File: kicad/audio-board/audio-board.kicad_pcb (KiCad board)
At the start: 2 copper layers, 0 parts

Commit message: [LIMA] audio board: board setup — 4-layer, 70x50 outline, holes, netclasses
In1/In2 added (planes), Edge.Cuts 70x50 mm R1 at (100,80), 4x M3 at 3.5 mm
from corners. Rules for JLCPCB 4-layer: 0.127 track/clearance, 0.3/0.5 via.
Netclasses: Default 0.2/0.15, Power 0.5/0.2 (rails, switch nodes, A2B bias
path), Aircraft 0.3/0.5 clearance (panel, electret, PV secondary, speakers,
K1 contacts). No footprints yet: the schematic sync needs the PCB editor open.

Co-Authored-By: Claude Opus 5.5 <noreply@anthropic.com>
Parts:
- added H1: MountingHole, MountingHole:MountingHole_3.2mm, F.Cu at (103.5, 83.5)
- added H2: MountingHole, MountingHole:MountingHole_3.2mm, F.Cu at (166.5, 83.5)
- added H3: MountingHole, MountingHole:MountingHole_3.2mm, F.Cu at (103.5, 126.5)
- added H4: MountingHole, MountingHole:MountingHole_3.2mm, F.Cu at (166.5, 126.5)
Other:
- board outline added: 70 x 50 mm
- copper layers 2 -> 4
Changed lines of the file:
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@@
 		(48 "B.Fab" user)
 		(49 "F.Fab" user)
+		(1 "In1.Cu" power)
+		(2 "In2.Cu" power)
 	)
 	(setup
@@
 	)
 	(net 0 "")
-)
+  (gr_line
+    (start 100 80)
+    (end 170 80)
+    (stroke (width 0.05) (type solid))
+    (layer "Edge.Cuts")
+  )
+  (gr_line
+    (start 170 80)
+    (end 170 130)
+    (stroke (width 0.05) (type solid))
+    (layer "Edge.Cuts")
+  )
+  (gr_line
+    (start 170 130)
+    (end 100 130)
+    (stroke (width 0.05) (type solid))
+    (layer "Edge.Cuts")
+  )
+  (gr_line
+    (start 100 130)
+    (end 100 80)
+    (stroke (width 0.05) (type solid))
+    (layer "Edge.Cuts")
+  )
+  (footprint "MountingHole:MountingHole_3.2mm"
+    (layer "F.Cu")
+    (at 103.5 83.5)
+    (attr exclude_from_pos_files)
+    (property "Reference" "H1"
+      (at 0 4.7 0)
+      (layer "F.SilkS")
+    )
+    (property "Value" "MountingHole"
+      (at 0 -4.7 0)
+      (layer "F.Fab")
+    )
+    (pad "" np_thru_hole circle (at 0 0) (size 3.7 3.7)
+      (drill 3.2)
+      (layers "*.Cu" "*.Mask")
+    )
+  )
+  (footprint "MountingHole:MountingHole_3.2mm"
+    (layer "F.Cu")
+    (at 166.5 83.5)
+    (attr exclude_from_pos_files)
+    (property "Reference" "H2"
+      (at 0 4.7 0)
+      (layer "F.SilkS")
+    )
+    (property "Value" "MountingHole"
+      (at 0 -4.7 0)
+      (layer "F.Fab")
+    )
+    (pad "" np_thru_hole circle (at 0 0) (size 3.7 3.7)
+      (drill 3.2)
+      (layers "*.Cu" "*.Mask")
+    )
+  )
+  (footprint "MountingHole:MountingHole_3.2mm"
+    (layer "F.Cu")
+    (at 103.5 126.5)
+    (attr exclude_from_pos_files)
+    (property "Reference" "H3"
+      (at 0 4.7 0)
+      (layer "F.SilkS")
+    )
+    (property "Value" "MountingHole"
+      (at 0 -4.7 0)
+      (layer "F.Fab")
+    )
+    (pad "" np_thru_hole circle (at 0 0) (size 3.7 3.7)
+      (drill 3.2)
+      (layers "*.Cu" "*.Mask")
+    )
+  )
+  (footprint "MountingHole:MountingHole_3.2mm"
+    (layer "F.Cu")
+    (at 166.5 126.5)
+    (attr exclude_from_pos_files)
+    (property "Reference" "H4"
+      (at 0 4.7 0)
+      (layer "F.SilkS")
+    )
+    (property "Value" "MountingHole"
+      (at 0 -4.7 0)
+      (layer "F.Fab")
+    )
+    (pad "" np_thru_hole circle (at 0 0) (size 3.7 3.7)
+      (drill 3.2)
+      (layers "*.Cu" "*.Mask")
+    )
+  ))

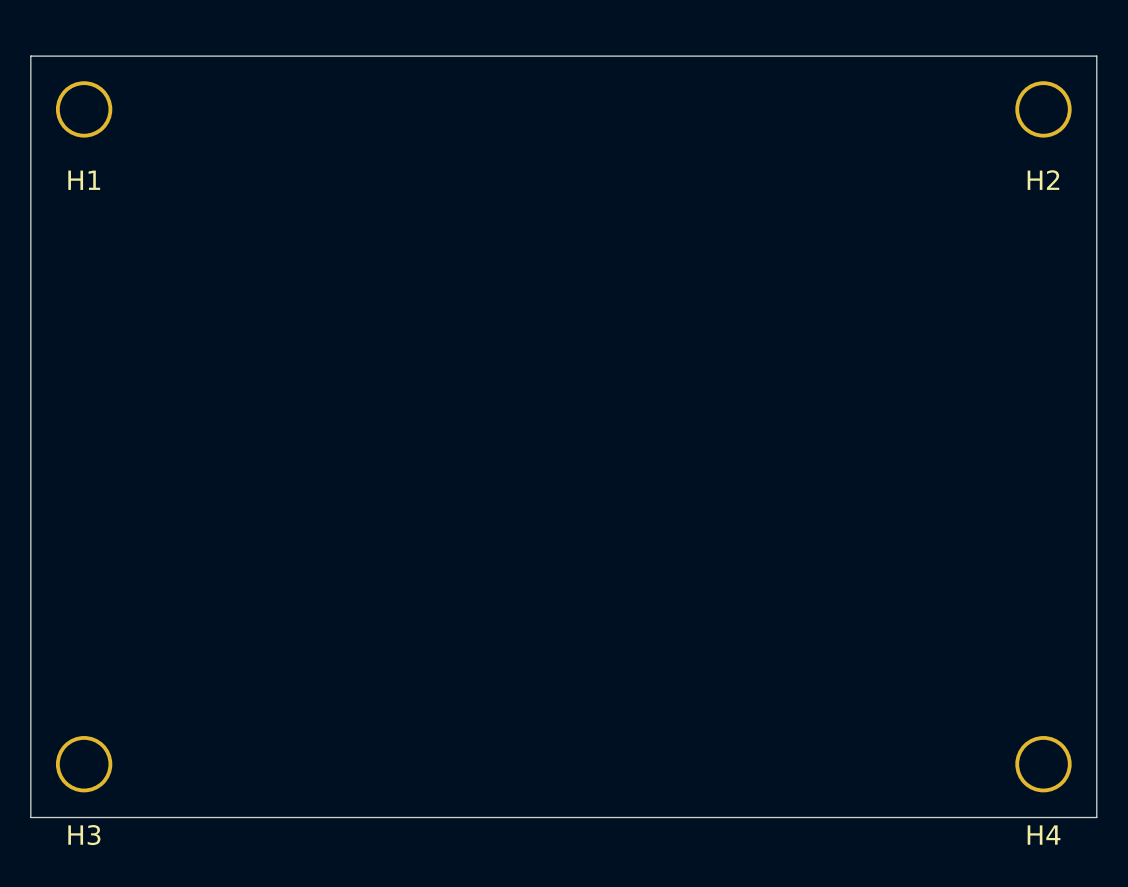
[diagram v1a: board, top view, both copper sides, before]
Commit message: [LIMA] audio board: all 121 parts placed (117 + 4 holes), placement DRC-clean
Synced from the schematic (one KiCad undo step), then placed by block:
host J1/J2 top edge, power top-left, hub centre with decoupling ring,
codec below-right, A2B node + bus filter + J3/J4 on the right edge,
K1 PhotoMOS by J5/J6 on the left edge, T2/T3/T4 along the bottom.
Placement table checked against real courtyards before applying.

Mounting holes H1-H4 now live in the schematic (Mechanical:MountingHole),
so future syncs don't trip on blank-identity board-only footprints.
Rules: min hole 0.2 (JLC 4-layer allows 0.15/0.25 via), Default and Power
clearance 0.127 (LFCSP corner pads sit 0.148 apart).

Checked on the saved file: DRC errors = 326 unconnected only; netlist ==
design file; ERC 0 errors. Not yet routed.

Co-Authored-By: Claude Opus 5.5 <noreply@anthropic.com>
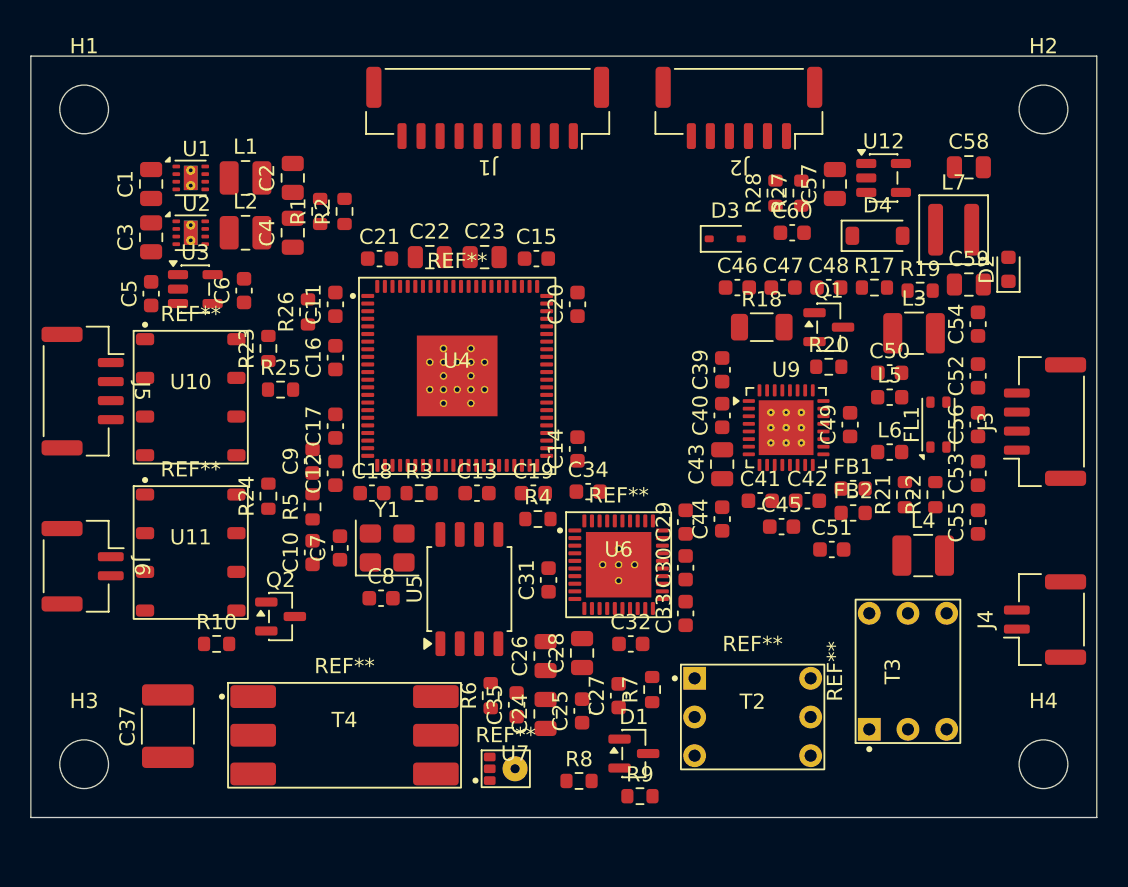
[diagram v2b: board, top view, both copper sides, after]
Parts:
- added C1: 10uF 25V, Capacitor_SMD:C_0805_2012Metric, F.Cu at (107.9, 88.4)
- added C10: 5.6nF C0G, Capacitor_SMD:C_0603_1608Metric, F.Cu at (118.5, 112.6)
- added C11: 100nF, Capacitor_SMD:C_0603_1608Metric, F.Cu at (120.0, 96.3)
- added C12: 100nF, Capacitor_SMD:C_0603_1608Metric, F.Cu at (120.0, 107.4)
- added C13: 100nF, Capacitor_SMD:C_0603_1608Metric, F.Cu at (129.3, 108.7)
- added C14: 100nF, Capacitor_SMD:C_0603_1608Metric, F.Cu at (135.9, 105.8)
- added C15: 100nF, Capacitor_SMD:C_0603_1608Metric, F.Cu at (133.2, 93.3)
- added C16: 100nF, Capacitor_SMD:C_0603_1608Metric, F.Cu at (120.0, 99.8)
- added C17: 100nF, Capacitor_SMD:C_0603_1608Metric, F.Cu at (120.0, 104.3)
- added C18: 100nF, Capacitor_SMD:C_0603_1608Metric, F.Cu at (122.4, 108.7)
- added C19: 100nF, Capacitor_SMD:C_0603_1608Metric, F.Cu at (133.0, 108.7)
- added C2: 22uF 10V, Capacitor_SMD:C_0805_2012Metric, F.Cu at (117.2, 88.0)
- added C20: 100nF, Capacitor_SMD:C_0603_1608Metric, F.Cu at (135.9, 96.3)
- added C21: 100nF, Capacitor_SMD:C_0603_1608Metric, F.Cu at (122.9, 93.3)
- added C22: 10uF, Capacitor_SMD:C_0805_2012Metric, F.Cu at (126.2, 93.2)
- added C23: 10uF, Capacitor_SMD:C_0805_2012Metric, F.Cu at (129.8, 93.2)
- added C24: 10uF, Capacitor_SMD:C_0805_2012Metric, F.Cu at (133.8, 123.2)
- added C25: 1uF, Capacitor_SMD:C_0603_1608Metric, F.Cu at (136.2, 123.0)
- added C26: 10uF, Capacitor_SMD:C_0805_2012Metric, F.Cu at (133.8, 119.4)
- added C27: 1uF, Capacitor_SMD:C_0603_1608Metric, F.Cu at (138.6, 122.0)
- added C28: 10uF, Capacitor_SMD:C_0805_2012Metric, F.Cu at (136.2, 119.2)
- added C29: 1uF, Capacitor_SMD:C_0603_1608Metric, F.Cu at (143.0, 110.6)
- added C3: 10uF 25V, Capacitor_SMD:C_0805_2012Metric, F.Cu at (107.9, 91.9)
- added C30: 100nF, Capacitor_SMD:C_0603_1608Metric, F.Cu at (143.0, 113.6)
- added C31: 100nF, Capacitor_SMD:C_0603_1608Metric, F.Cu at (134.0, 114.4)
- added C32: 100nF, Capacitor_SMD:C_0603_1608Metric, F.Cu at (139.4, 118.6)
- added C33: 100nF, Capacitor_SMD:C_0603_1608Metric, F.Cu at (143.0, 116.6)
- added C34: 100nF, Capacitor_SMD:C_0603_1608Metric, F.Cu at (136.6, 108.6)
- added C35: 1uF, Capacitor_SMD:C_0603_1608Metric, F.Cu at (131.9, 122.6)
- added C37: 220nF film, Capacitor_SMD:C_1812_4532Metric, F.Cu at (109.0, 124.0)
- added C39: 4.7uF, Capacitor_SMD:C_0603_1608Metric, F.Cu at (145.4, 100.6)
- added C4: 22uF 6.3V, Capacitor_SMD:C_0805_2012Metric, F.Cu at (117.2, 91.6)
- added C40: 100nF, Capacitor_SMD:C_0603_1608Metric, F.Cu at (145.4, 103.6)
- added C41: 4.7uF, Capacitor_SMD:C_0603_1608Metric, F.Cu at (147.9, 109.2)
- added C42: 100nF, Capacitor_SMD:C_0603_1608Metric, F.Cu at (151.0, 109.2)
- added C43: 10uF 25V, Capacitor_SMD:C_0805_2012Metric, F.Cu at (145.4, 106.8)
- added C44: 100nF, Capacitor_SMD:C_0603_1608Metric, F.Cu at (145.4, 110.4)
- added C45: 100nF, Capacitor_SMD:C_0603_1608Metric, F.Cu at (149.3, 110.9)
- added C46: 33nF, Capacitor_SMD:C_0603_1608Metric, F.Cu at (146.4, 95.2)
- added C47: 15nF, Capacitor_SMD:C_0603_1608Metric, F.Cu at (149.4, 95.2)
- added C48: 3.3nF, Capacitor_SMD:C_0603_1608Metric, F.Cu at (152.4, 95.2)
- added C49: 12pF C0G, Capacitor_SMD:C_0603_1608Metric, F.Cu at (153.8, 104.2)
- added C5: 2.2uF 25V, Capacitor_SMD:C_0603_1608Metric, F.Cu at (107.9, 95.6)
- added C50: 27pF C0G, Capacitor_SMD:C_0603_1608Metric, F.Cu at (156.4, 100.8)
- added C51: 33nF, Capacitor_SMD:C_0603_1608Metric, F.Cu at (152.6, 112.4)
- added C52: 10nF, Capacitor_SMD:C_0603_1608Metric, F.Cu at (162.2, 101.0)
- added C53: 10nF, Capacitor_SMD:C_0603_1608Metric, F.Cu at (162.2, 107.4)
- added C54: 33nF, Capacitor_SMD:C_0603_1608Metric, F.Cu at (162.2, 97.6)
- added C55: 33nF, Capacitor_SMD:C_0603_1608Metric, F.Cu at (162.2, 110.6)
- added C56: 33nF, Capacitor_SMD:C_0603_1608Metric, F.Cu at (162.2, 104.2)
- added C57: 10uF 16V, Capacitor_SMD:C_0805_2012Metric, F.Cu at (152.8, 88.4)
- added C58: 10uF 25V, Capacitor_SMD:C_0805_2012Metric, F.Cu at (161.6, 87.3)
- added C59: 10uF 25V, Capacitor_SMD:C_0805_2012Metric, F.Cu at (161.6, 95.0)
- added C6: 2.2uF 10V, Capacitor_SMD:C_0603_1608Metric, F.Cu at (114.0, 95.4)
- added C60: 330pF, Capacitor_SMD:C_0603_1608Metric, F.Cu at (150.0, 91.6)
- added C7: 100nF, Capacitor_SMD:C_0603_1608Metric, F.Cu at (120.3, 112.3)
- added C8: 100nF, Capacitor_SMD:C_0603_1608Metric, F.Cu at (123.0, 115.6)
- added C9: 150pF C0G, Capacitor_SMD:C_0603_1608Metric, F.Cu at (118.5, 106.6)
- added D1: BAT54S, Package_TO_SOT_SMD:SOT-23, F.Cu at (139.6, 125.8)
- added D2: CDBU0130L, Diode_SMD:D_0603_1608Metric, F.Cu at (164.2, 94.0)
- added D3: ZLLS400, Diode_SMD:D_SOD-323, F.Cu at (145.6, 92.0)
- added D4: MBR0520, Diode_SMD:D_SOD-123, F.Cu at (155.6, 91.8)
- added FB1: 1000R@100MHz, Inductor_SMD:L_0603_1608Metric, F.Cu at (154.0, 108.4)
- added FB2: 1000R@100MHz, Inductor_SMD:L_0603_1608Metric, F.Cu at (154.0, 110.0)
- added FL1: 2600R@100MHz CMC, Inductor_SMD:L_CommonModeChoke_Coilank_ACM3216, F.Cu at (159.6, 104.2)
- added J1: HOST_J3 (AeroNode), Connector_JST:JST_GH_SM10B-GHS-TB_1x10-1MP_P1.25mm_Horizontal, F.Cu at (130.0, 83.4)
- added J2: HOST_J4 (AeroNode), Connector_JST:JST_GH_SM06B-GHS-TB_1x06-1MP_P1.25mm_Horizontal, F.Cu at (146.5, 83.4)
- added J3: CUP_L (A2B + speaker), Connector_JST:JST_GH_SM04B-GHS-TB_1x04-1MP_P1.25mm_Horizontal, F.Cu at (166.6, 104.0)
- added J4: CUP_R (speaker), Connector_JST:JST_GH_SM02B-GHS-TB_1x02-1MP_P1.25mm_Horizontal, F.Cu at (166.6, 117.0)
- added J5: PANEL (ear + mic), Connector_JST:JST_GH_SM04B-GHS-TB_1x04-1MP_P1.25mm_Horizontal, F.Cu at (103.4, 102.0)
- added J6: FAILSAFE_ELECTRET, Connector_JST:JST_GH_SM02B-GHS-TB_1x02-1MP_P1.25mm_Horizontal, F.Cu at (103.4, 113.5)
- added L1: 2.2uH, Inductor_SMD:L_1008_2520Metric, F.Cu at (114.1, 88.0)
- added L2: 2.2uH, Inductor_SMD:L_1008_2520Metric, F.Cu at (114.1, 91.6)
- added L3: 3.3uH, Inductor_SMD:L_1210_3225Metric, F.Cu at (158.0, 98.2)
- added L4: 3.3uH, Inductor_SMD:L_1210_3225Metric, F.Cu at (158.6, 112.8)
- added L5: 180nH, Inductor_SMD:L_0603_1608Metric, F.Cu at (156.4, 102.4)
- added L6: 180nH, Inductor_SMD:L_0603_1608Metric, F.Cu at (156.4, 106.0)
- added L7: 10uH 1.5A, Inductor_SMD:L_Coilcraft_XAL4030-XXX, F.Cu at (160.6, 91.4)
- added Q1: AO3401A, Package_TO_SOT_SMD:SOT-23, F.Cu at (152.4, 97.8)
- added Q2: 2N7002, Package_TO_SOT_SMD:SOT-23, F.Cu at (116.4, 116.8)
- added R1: 49.9k 1%, Resistor_SMD:R_0603_1608Metric, F.Cu at (119.0, 90.2)
- added R10: 10k, Resistor_SMD:R_0603_1608Metric, F.Cu at (112.2, 118.6)
- added R17: 33k, Resistor_SMD:R_0603_1608Metric, F.Cu at (155.4, 95.2)
- added R18: 1R 1206, Resistor_SMD:R_1206_3216Metric, F.Cu at (148.0, 97.8)
- added R19: 3.3k, Resistor_SMD:R_0603_1608Metric, F.Cu at (158.4, 95.4)
- added R2: 100k 1%, Resistor_SMD:R_0603_1608Metric, F.Cu at (120.6, 90.2)
- added R20: 1k, Resistor_SMD:R_0603_1608Metric, F.Cu at (152.4, 100.4)
- added R21: 120R, Resistor_SMD:R_0603_1608Metric, F.Cu at (157.4, 108.8)
- added R22: 120R, Resistor_SMD:R_0603_1608Metric, F.Cu at (159.4, 108.8)
- added R23: 390R, Resistor_SMD:R_0603_1608Metric, F.Cu at (115.6, 99.2)
- added R24: 390R, Resistor_SMD:R_0603_1608Metric, F.Cu at (115.6, 108.9)
- added R25: 100k, Resistor_SMD:R_0603_1608Metric, F.Cu at (116.4, 101.9)
- added R26: 0R (VDRIVE to GND: external DVDD), Resistor_SMD:R_0603_1608Metric, F.Cu at (118.2, 96.8)
- added R27: 73.2k 1%, Resistor_SMD:R_0603_1608Metric, F.Cu at (150.6, 89.0)
- added R28: 13.3k 1%, Resistor_SMD:R_0603_1608Metric, F.Cu at (148.9, 89.0)
- added R3: 100k, Resistor_SMD:R_0603_1608Metric, F.Cu at (125.5, 108.7)
- added R4: 10k, Resistor_SMD:R_0603_1608Metric, F.Cu at (133.3, 110.4)
- added R5: 4.3k 1%, Resistor_SMD:R_0603_1608Metric, F.Cu at (118.5, 109.6)
- added R6: 100R, Resistor_SMD:R_0603_1608Metric, F.Cu at (130.2, 122.0)
- added R7: 10k, Resistor_SMD:R_0603_1608Metric, F.Cu at (140.8, 121.6)
- added R8: 10k, Resistor_SMD:R_0603_1608Metric, F.Cu at (136.0, 127.6)
- added R9: 0R, Resistor_SMD:R_0603_1608Metric, F.Cu at (140.0, 128.6)
- added T2: Triad SP-74 (cup L), Triad:Triad_SP-74_THT_10.4x7.9mm_P2.54mm, F.Cu at (147.4, 123.4)
- added T3: Triad SP-74 (cup R), Triad:Triad_SP-74_THT_10.4x7.9mm_P2.54mm, F.Cu at (157.6, 120.4)
- added T4: Bourns SM-LP-5001 (600:600), Bourns:Bourns_SM-LP-5001_12.8x9.0mm_P2.54mm, F.Cu at (120.6, 124.6)
- added U1: TPS62162DSG, Package_SON:WSON-8-1EP_2x2mm_P0.5mm_EP0.9x1.6mm_ThermalVias, F.Cu at (110.5, 88.0)
- added U10: AQW612S (K1 mic-hi), Panasonic:Panasonic_GU-SOP8_4.4x9.37mm_P2.54mm_AQW61xS, F.Cu at (110.5, 102.4)
- added U11: AQW612S (K1 mic-lo), Panasonic:Panasonic_GU-SOP8_4.4x9.37mm_P2.54mm_AQW61xS, F.Cu at (110.5, 112.6)
- added U12: LM2731XMF (8 V A2B bus), Package_TO_SOT_SMD:SOT-23-5, F.Cu at (156.0, 88.0)
- added U2: TPS62160DSG, Package_SON:WSON-8-1EP_2x2mm_P0.5mm_EP0.9x1.6mm_ThermalVias, F.Cu at (110.5, 91.6)
- added U3: ADP7118AUJZ-3.3-R7, Package_TO_SOT_SMD:TSOT-23-5, F.Cu at (110.8, 95.3)
- added U4: ADAU1467, AnalogDevices:AD_LFCSP-88-1EP_12x12mm_P0.5mm_EP5.3x5.3mm_CP-88-10, F.Cu at (128.0, 101.0)
- added U5: W25Q32JVSS, Package_SO:SOIC-8_5.3x5.3mm_P1.27mm, F.Cu at (128.8, 115.0)
- added U6: ADAU1372, AnalogDevices:AD_LFCSP-40-1EP_6x6mm_P0.5mm_EP4.3x4.3mm_CP-40-10, F.Cu at (138.6, 113.4)
- added U7: IM68A130A, Infineon:Infineon_PG-TLGA-4-2_3.35x2.5mm_IM68A130A, F.Cu at (131.8, 126.8)
- added U9: AD2428WBCPZ, Package_DFN_QFN:QFN-32-1EP_5x5mm_P0.5mm_EP3.6x3.6mm_ThermalVias, F.Cu at (149.6, 104.4)
- added Y1: SiT8008 12.288MHz 3.3V, Oscillator:Oscillator_SMD_SiT_PQFN-4Pin_3.2x2.5mm, F.Cu at (123.4, 112.3)
- H1, H2, H3, H4: value MountingHole -> M3; footprint MountingHole:MountingHole_3.2mm -> MountingHole:MountingHole_3.2mm_M3

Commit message: [LIMA] audio board: inner planes In1 GND / In2 +3V3, cut back from the aircraft side
Both planes stop short of J5/J6, the K1 PhotoMOS outputs and T4/R10/C37
(left strip x<116.8 from y 96, bottom-left x<129.6 from y 117.5).

Co-Authored-By: Claude Opus 5.5 <noreply@anthropic.com>
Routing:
- added copper zone on In2.Cu, net /+3V3
- added copper zone on In1.Cu, net /GND
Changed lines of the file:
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@@
 	)
 	(embedded_fonts no)
-)
+  (zone (net "/GND") (layers "In1.Cu")
+    (hatch edge 0.508)
+    (connect_pads (clearance 0.2))
+    (min_thickness 0.2)
+    (fill yes (thermal_gap 0.5) (thermal_bridge_width 0.5))
+    (polygon (pts
+      (xy 100.5 80.5)
+      (xy 169.5 80.5)
+      (xy 169.5 129.5)
+      (xy 129.6 129.5)
+      (xy 129.6 117.5)
+      (xy 116.8 117.5)
+      (xy 116.8 96)
+      (xy 100.5 96)
+    ))
+  )
+  (zone (net "/+3V3") (layers "In2.Cu")
+    (hatch edge 0.508)
+    (connect_pads (clearance 0.2))
+    (min_thickness 0.2)
+    (fill yes (thermal_gap 0.5) (thermal_bridge_width 0.5))
+    (polygon (pts
+      (xy 100.5 80.5)
+      (xy 169.5 80.5)
+      (xy 169.5 129.5)
+      (xy 129.6 129.5)
+      (xy 129.6 117.5)
+      (xy 116.8 117.5)
+      (xy 116.8 96)
+      (xy 100.5 96)
+    ))
+  ))

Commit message: [LIMA] audio board PCB: new FFC J1 synced and placed top-centre
Old J1 (10-pin) and J2 (6-pin) removed from the board, new Cvilux CF31241
J1 added by schematic sync and placed at (138, 85.7) rot 180 so the cable
enters from the top edge. Saved-file DRC: errors are unconnected only.

Co-Authored-By: Claude Opus 5.5 <noreply@anthropic.com>
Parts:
- removed J2: HOST_J4 (AeroNode), Connector_JST:JST_GH_SM06B-GHS-TB_1x06-1MP_P1.25mm_Horizontal
- J1: value HOST_J3 (AeroNode) -> AERONODE_FFC (mates J9); footprint Connector_JST:JST_GH_SM10B-GHS-TB_1x10-1MP_P1.25mm_Horizontal -> Cvilux:Cvilux_CF31241D0R0-05-NH_1x24-1MP_P0.5mm_Horizontal
- moved J1 8.32 mm to (138.0, 85.7)
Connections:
- J1 pad 10: /VBAT -> /HOST_SDO0
- J1 pad 2: /I2S_WS -> /VBAT
- J1 pad 3: /I2S_BCLK -> /GND
- J1 pad 4: /HOST_SDI0 -> /I2C_SDA
- J1 pad 5: /HOST_SDO0 -> /I2C_SCL
- J1 pad 6: /HOST_SDI1 -> /GND
- J1 pad 7: /HOST_SDO1 -> /CTL_MIC
- J1 pad 8: /I2C_SCL -> /CTL_SPKR
- J1 pad 9: /I2C_SDA -> unconnected-(J1-Pin_9-Pad9)
- J1 pad MP: (no net) -> /GND
